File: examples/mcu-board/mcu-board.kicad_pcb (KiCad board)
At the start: 2 copper layers, 60 x 30 mm, 15 parts, among them J1 5V_IN, J2 PROG/IO, SW1 Reset, U1 MCU, U2 AMS1117-3.3

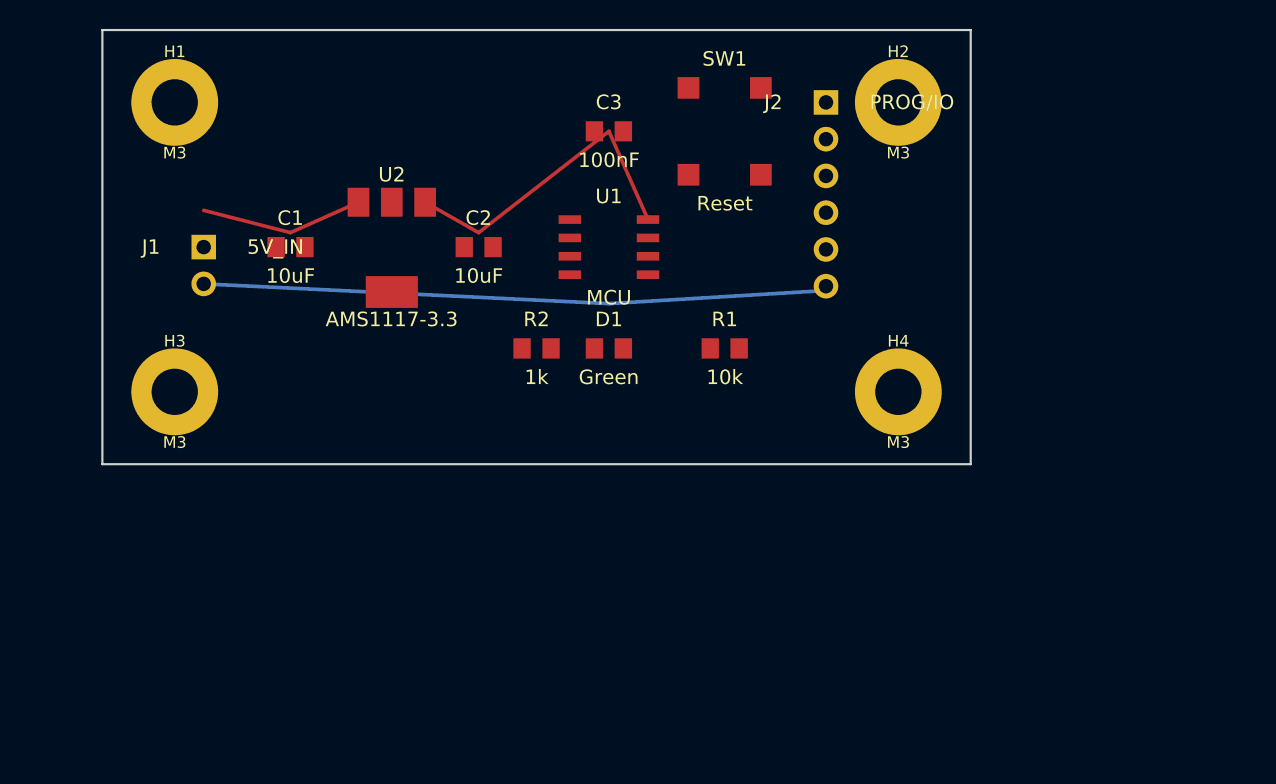
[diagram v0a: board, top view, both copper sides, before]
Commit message: examples/mcu-board: lay out for expansion (regions, spare GPIO, GND fan)
Iteration on the mcu-board example so it works as a "real board you'd
extend" rather than a one-shot snapshot. Three concrete changes:

Schematic — break out every spare MCU GPIO (PA1, PA2, PA3, PA5) as a
named-net label stub at the MCU pin. Adding a peripheral later means
dropping in a component with a label on the matching net; no rerouting
of existing wires.

PCB — redo the layout with three named silkscreen regions
("POWER" / "MCU" / "PERIPHERALS") matching the left-to-right power
flow, on a larger 80×50 mm board. The bottom-third of the board is
intentionally left empty (silkscreen "expansion" marker) so an
added peripheral can land somewhere with mounting holes still
unobstructed at the corners.

PCB — replace the old single-segment B.Cu trace with a fan of GND
drops from each GND-bearing pad to a horizontal spine at the bottom
edge. kicad-cli can't compute zone fills offline, so this is the
closest we can get to "looks like a real GND pour" while staying
fully renderable from the CLI.

Co-Authored-By: Claude Opus 4.7 (1M context) <noreply@anthropic.com>
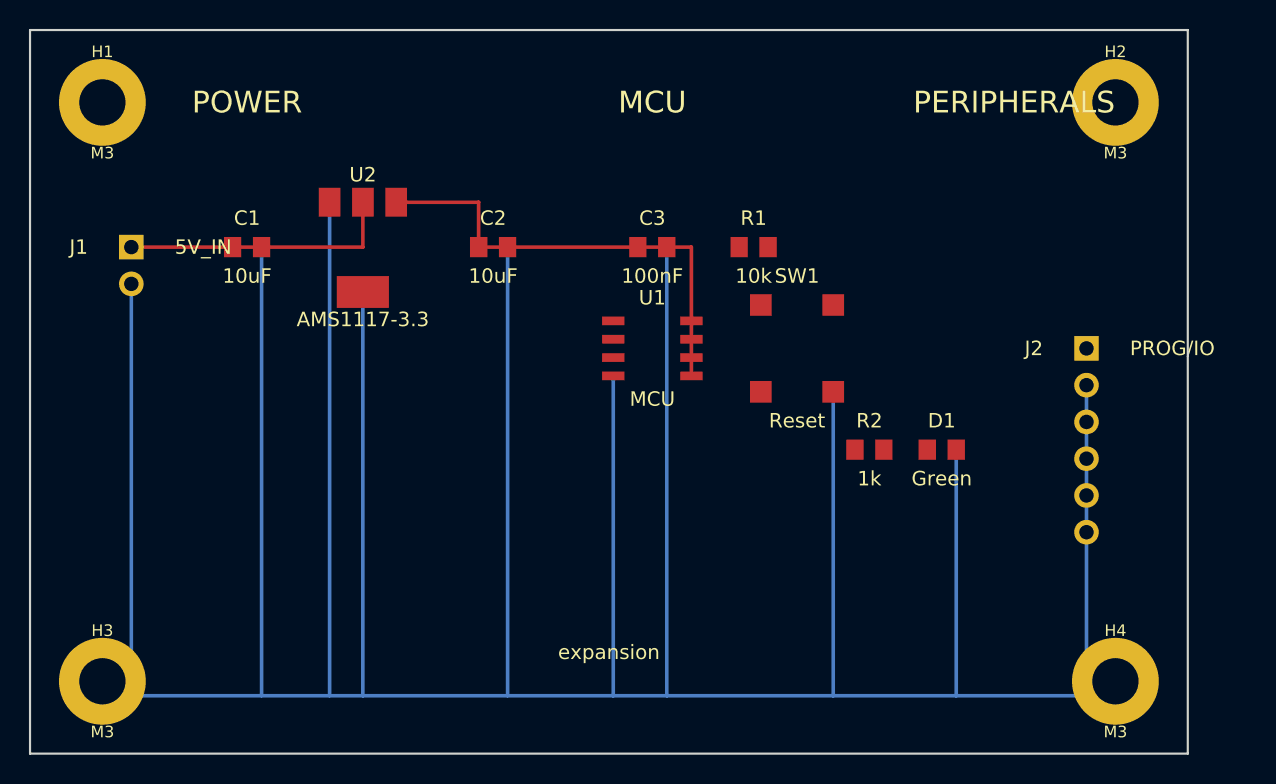
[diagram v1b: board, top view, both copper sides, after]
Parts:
- R1: renamed from SW1; value Reset -> 10k; footprint Button_Switch_SMD:SW_SPST_TL3342 -> Resistor_SMD:R_0805_2012Metric
- SW1: renamed from R1; value 10k -> Reset; footprint Resistor_SMD:R_0805_2012Metric -> Button_Switch_SMD:SW_SPST_TL3342
- moved H4 25.0 mm to (165.0, 140.0)
- moved J2 24.8 mm to (163.0, 117.0)
- moved D1 24.0 mm to (153.0, 124.0)
- moved R2 24.0 mm to (148.0, 124.0)
- moved H3 20.6 mm to (95.0, 140.0)
- moved H2 15.0 mm to (165.0, 100.0)
- moved C3 8.54 mm to (133.0, 110.0)
- moved R1 8.25 mm to (140.0, 110.0)
- moved U1 7.62 mm to (133.0, 117.0)
- moved H1 5.00 mm to (95.0, 100.0)
- moved J1 5.00 mm to (97.0, 110.0)
- moved SW1 5.00 mm to (143.0, 117.0)
- moved C1 3.00 mm to (105.0, 110.0)
- moved U2 2.00 mm to (113.0, 110.0)
- moved C2 1.00 mm to (122.0, 110.0)
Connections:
- D1 pad 1: LED_A -> PA4_OUT
- R1 pad 1: RST -> +3V3
- R1 pad 2: GND -> RST
- R2 pad 1: +3V3 -> LED_A
- R2 pad 2: LED_A -> PA4_OUT
- SW1 pad 1: +3V3 -> RST
- SW1 pad 2: RST -> GND
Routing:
- net GND: track 54.4 -> 331.0 mm
- net VIN: track 0.00 -> 19.1 mm
- net +3V3: track 22.3 -> 32.4 mm
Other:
- board size 60 x 30 mm -> 80 x 50 mm
- board text added: "MCU"
- board text added: "PERIPHERALS"
- board text added: "POWER"
- board text added: "expansion"

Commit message: examples/mcu-board: polish silkscreen / label placement
Render-feedback driven cleanup of the previous layout pass:

- "PERIPHERALS" silkscreen overflowed the right board edge → renamed
  to "I/O" and the region X positions are pre-computed to centre each
  label on its zone (kicad-cli rejects `(justify center)` on top-level
  gr_text, so all silkscreen text is left-justified).
- J1's value ("5V_IN") was rendered off the *left* board edge because
  its silkscreen labels were always on the connector's left side. The
  fp_header helper now takes a `side="left"|"right"` arg; J1 (near
  the left edge) uses `side="right"`, J2 (near the right edge) keeps
  the default `side="left"`. Both ref and value sit on the same side.
- SW1 ("Reset") and R2 ("1k") collided on the silkscreen because their
  text positions happened to coincide. R2 + D1 moved one row down, so
  the reset network gets the upper peripheral row to itself.
- Schematic stubs from MCU pins to named-net labels were 4 mm long;
  bumped to 6 mm so the label glyphs no longer crowd the pin-number
  glyphs at the symbol edge.

Co-Authored-By: Claude Opus 4.7 (1M context) <noreply@anthropic.com>
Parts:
- moved R2 5.83 mm to (143.0, 127.0)
- moved SW1 5.00 mm to (148.0, 117.0)
- moved D1 3.00 mm to (153.0, 127.0)
- moved J2 3.00 mm to (160.0, 117.0)
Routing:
- net GND: track 331.0 -> 325.0 mm
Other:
- board text added: "I/O"
- board text removed: "PERIPHERALS"
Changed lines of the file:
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@@
 		(at 97 110)
 		(property "Reference" "J1"
-			(at -3 0 0)
-			(layer "F.SilkS")
-			(effects
-				(font
-					(size 1 1)
-					(thickness 0.15)
-				)
-				(justify right)
+			(at 3 -2 0)
+			(layer "F.SilkS")
+			(effects
+				(font
+					(size 1 1)
+					(thickness 0.15)
+				)
+				(justify left)
 			)
 		)
 		(property "Value" "5V_IN"
-			(at 3 0 0)
+			(at 3 4.54 0)
 			(layer "F.SilkS")
 			(effects
@@
 	(footprint "Button_Switch_SMD:SW_SPST_TL3342"
 		(layer "F.Cu")
-		(at 143 117)
+		(at 148 117)
 		(property "Reference" "SW1"
 			(at 0 -5 0)
@@
 	(footprint "Resistor_SMD:R_0805_2012Metric"
 		(layer "F.Cu")
-		(at 148 124)
+		(at 143 127)
 		(property "Reference" "R2"
 			(at 0 -2 0)
@@
 	(footprint "Resistor_SMD:LED_0805_2012Metric"
 		(layer "F.Cu")
-		(at 153 124)
+		(at 153 127)
 		(property "Reference" "D1"
 			(at 0 -2 0)
@@
 	(footprint "Connector_PinHeader_2.54mm:PinHeader_1x06"
 		(layer "F.Cu")
-		(at 163 117)
+		(at 160 117)
 		(property "Reference" "J2"
-			(at -3 0 0)
+			(at -3 -2 0)
 			(layer "F.SilkS")
 			(effects
@@
 		)
 		(property "Value" "PROG/IO"
-			(at 3 0 0)
-			(layer "F.SilkS")
-			(effects
-				(font
-					(size 1 1)
-					(thickness 0.15)
-				)
-				(justify left)
+			(at -3 14.7 0)
+			(layer "F.SilkS")
+			(effects
+				(font
+					(size 1 1)
+					(thickness 0.15)
+				)
+				(justify right)
 			)
 		)
@@
 	)
 	(gr_text "expansion"
-		(at 130 138 0)
+		(at 123 138 0)
 		(layer "F.SilkS")
 		(effects
@@
 	)
 	(gr_text "POWER"
-		(at 105 100 0)
+		(at 100 100 0)
 		(layer "F.SilkS")
 		(effects
@@
 	)
 	(gr_text "MCU"
-		(at 133 100 0)
+		(at 130 100 0)
 		(layer "F.SilkS")
 		(effects
@@
 		)
 	)
-	(gr_text "PERIPHERALS"
-		(at 158 100 0)
+	(gr_text "I/O"
+		(at 154 100 0)
 		(layer "F.SilkS")
 		(effects
@@
 	)
 	(segment
-		(start 145.5 120)
-		(end 145.5 141)
+		(start 150.5 120)
+		(end 150.5 141)
 		(width 0.25)
 		(layer "B.Cu")
@@
 	)
 	(segment
-		(start 154 124)
+		(start 154 127)
 		(end 154 141)
 		(width 0.25)
@@
 	)
 	(segment
-		(start 163 119.54)
-		(end 163 141)
+		(start 160 119.54)
+		(end 160 141)
 		(width 0.25)
 		(layer "B.Cu")
@@
 	(segment
 		(start 97 141)
-		(end 163 141)
+		(end 160 141)
 		(width 0.25)
 		(layer "B.Cu")
